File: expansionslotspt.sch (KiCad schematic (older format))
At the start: 9 parts, among them U14 74LS08, U15 74LS08, U16 74LS08

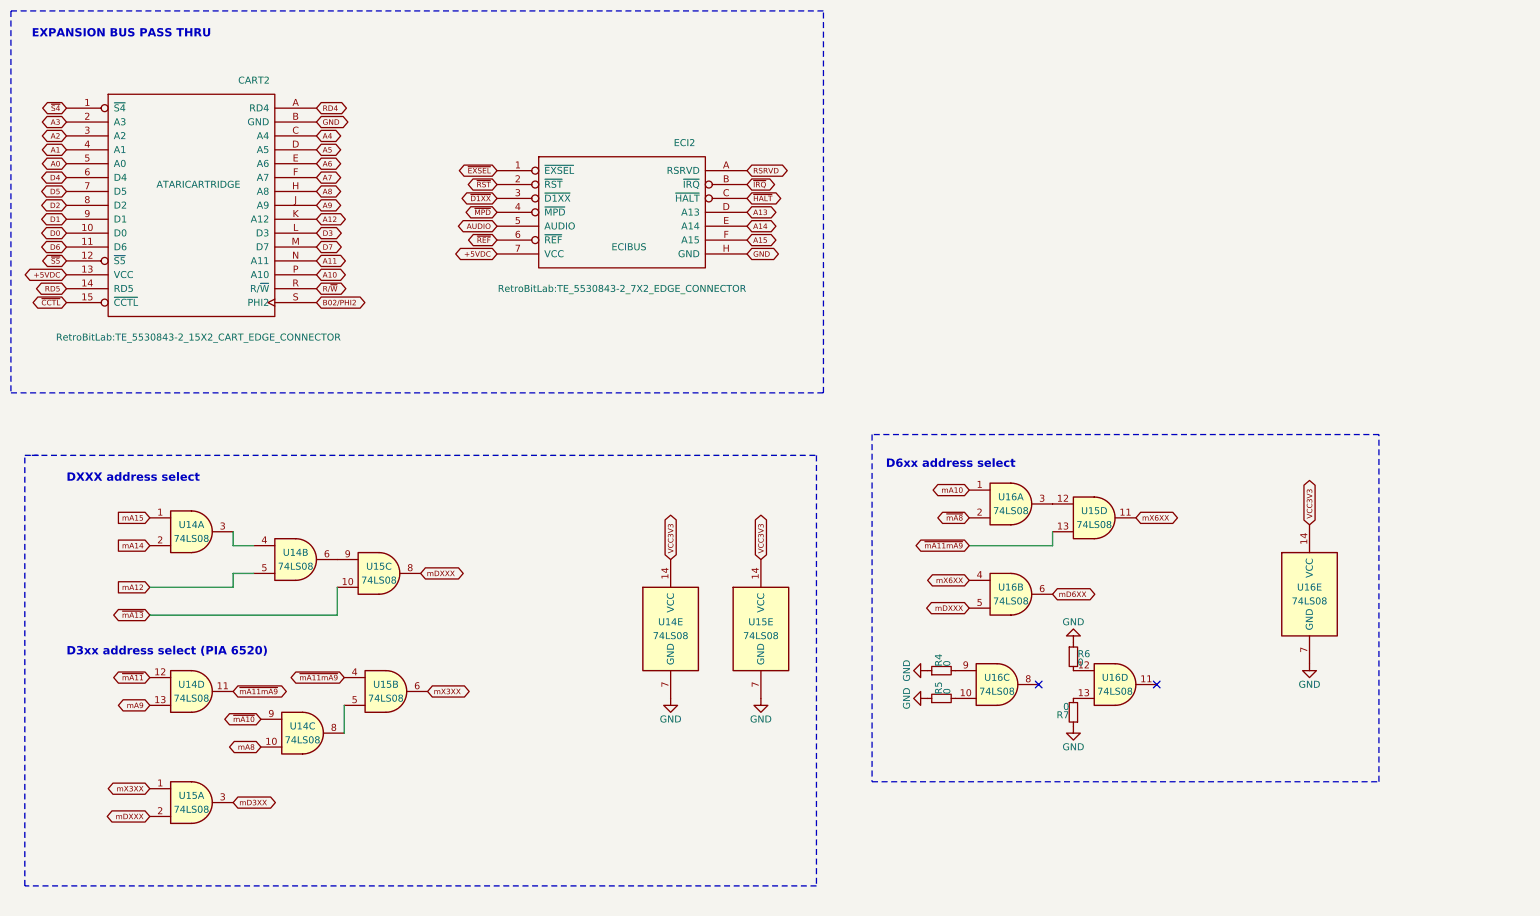
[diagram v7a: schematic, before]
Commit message: Upgraded with the latest infos
Now there is no logic for address/decoding. All is done inside the
microprocessor. This is a semi-final release.
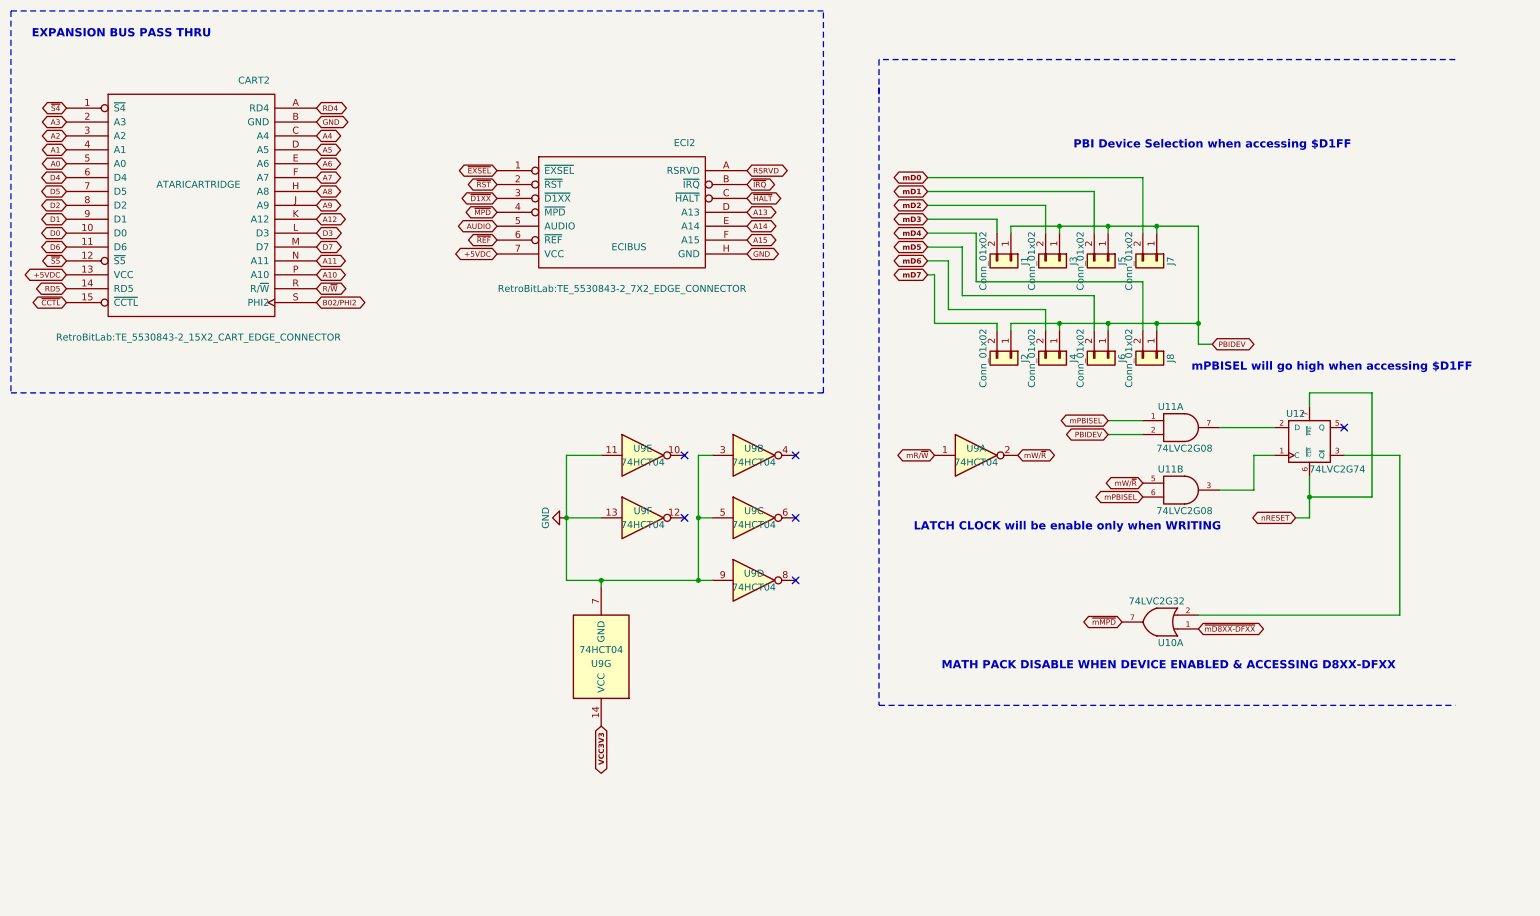
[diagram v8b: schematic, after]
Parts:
- removed R4, R5, R6, R7: 0, Resistors_SMD:R_1206_HandSoldering, symbol R_Small
- removed U14, U15, U16: 74LS08, Housings_SSOP:SSOP-14_5.3x6.2mm_Pitch0.65mm, symbol 74LS08
- added J1, J2, J3, J4, J5, J6, J7, J8: Conn_01x02, Pin_Headers:Pin_Header_Straight_1x02, symbol Conn_01x02
- added U10: 74LVC2G32, Housings_SSOP:TSSOP-8_3x3mm_Pitch0.65mm, symbol 74LVC2G32
- added U11: 74LVC2G08, Housings_SSOP:TSSOP-8_3x3mm_Pitch0.65mm, symbol 74LVC2G08
- added U12: 74LVC2G74, Housings_SSOP:TSSOP-8_3x3mm_Pitch0.65mm, symbol 74LVC2G74
- added U9: 74HCT04, Housings_SSOP:SSOP-14_5.3x6.2mm_Pitch0.65mm, symbol 74HCT04
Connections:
- net GND: now also U10.4 (GND), U11.4 (GND), U11.4 (GND), U12.4 (GND), U9.11, U9.13, U9.3, U9.5, U9.7 (GND), U9.9
- net VCC3V3: now also U9.14 (VCC)
- new net: U11.3, U12.1 (C)
- new net: U11.7, U12.2 (D)
- new net: U10.2, U12.3 (~Q)
- new net PBIDEV: J1.1 (Pin_1), J2.1 (Pin_1), J3.1 (Pin_1), J4.1 (Pin_1), J5.1 (Pin_1), J6.1 (Pin_1), J7.1 (Pin_1), J8.1 (Pin_1), U11.2
- new net VCC: U10.8 (VCC), U11.8 (VCC), U11.8 (VCC), U12.8 (VCC)
- new net mD0: J7.2 (Pin_2)
- new net mD1: J5.2 (Pin_2)
- new net mD2: J3.2 (Pin_2)
- new net mD3: J1.2 (Pin_2)
- new net mD4: J8.2 (Pin_2)
- new net mD5: J6.2 (Pin_2)
- new net mD6: J4.2 (Pin_2)
- new net mD7: J2.2 (Pin_2)
- new net mPBISEL: U11.1, U11.6
- new net mR/~W: U9.1
- new net mW/~R: U11.5, U9.2
- new net nRESET: U12.6 (~CLR), U12.7 (~PRE)
- new net ~mD8XX-DFXX: U10.1
- new net ~mMPD: U10.7
- no-connect marks 2 -> 6
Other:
- note added: "LATCH CLOCK will be enable only when WRITING"
- note added: "MATH PACK DISABLE WHEN DEVICE ENABLED & ACCESSING D8XX-DFXX"
- note added: "PBI Device Selection when accessing $D1FF"
- note added: "mPBISEL will go high when accessing $D1FF"
- note removed: "D3xx address select (PIA 6520)"
- note removed: "D6xx address select"
- note removed: "DXXX address select"
